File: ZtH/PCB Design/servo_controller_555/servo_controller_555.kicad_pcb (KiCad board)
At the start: 2 copper layers, 60 x 50 mm, 20 parts, among them J1 SERVO, J2 VIN, U1 LM555xN, U2 AMS1117

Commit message: a
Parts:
- moved U2 119.1 mm to (68.3, 85.0)
- moved D2 95.5 mm to (66.5, 72.0)
- moved C3 94.5 mm to (67.5, 77.0), turned to 180 degrees
- moved D3 92.9 mm to (68.0, 95.0), turned to 180 degrees
- moved D4 91.0 mm to (57.0, 93.5), turned to 180 degrees
- moved R3 88.4 mm to (62.0, 69.4), turned to -90 degrees
- moved U1 85.4 mm to (95.5, 93.1), turned to 180 degrees
- moved R4 78.9 mm to (68.5, 92.0), turned to 180 degrees
- moved C1 73.6 mm to (98.4, 90.6), turned to -90 degrees
- moved C2 73.0 mm to (90.4, 97.6)
- moved R2 64.7 mm to (83.8, 75.6)
- moved R1 62.6 mm to (83.9, 78.1)
- moved D1 56.5 mm to (83.9, 81.1)
- moved RV1 13.0 mm to (80.6, 107.5), turned to 90 degrees
- moved J1 1.46 mm to (105.0, 82.5)
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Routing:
- net +5V: track 0.00 -> 114.9 mm
- net GND: track 0.00 -> 58.1 mm, vias 0 -> 1
- net Net-(R2-Pad1): track 0.00 -> 34.0 mm
- net Net-(D1-K): track 0.00 -> 23.1 mm
- net +12V: track 0.00 -> 17.6 mm
- net Net-(D1-A): track 0.00 -> 16.5 mm
- net Net-(J1-Pin_3): track 0.00 -> 9.69 mm
- net Net-(D4-A): track 0.00 -> 7.62 mm
- net Net-(D2-K): track 0.00 -> 5.55 mm
- net Net-(D3-K): track 0.00 -> 3.41 mm
- added copper zone on B.Cu, net GND

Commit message: updated pcb
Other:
- board text added: "Theo Devos-Vernes c3479858 15/08/2026"
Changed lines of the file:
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@@
 	)
 	(paper "A4")
+	(title_block
+		(title "servo controller 555 pcb")
+		(company "NUTeams")
+		(comment 1 "Theo Devos-Vernes")
+		(comment 2 "c3479858")
+	)
 	(layers
 		(0 "F.Cu" signal)
@@
 		(layer "Edge.Cuts")
 	)
+	(gr_text "Theo Devos-Vernes\nc3479858\n15/08/2026"
+		(at 78 67 0)
+		(layer "F.SilkS")
+		(effects
+			(font
+				(size 1 1)
+				(thickness 0.1)
+			)
+			(justify left bottom)
+		)
+	)
 	(segment
 		(start 87.88 88)
@@
 	)
 	(segment
+		(start 71.5 85)
+		(end 79.58 93.08)
+		(width 0.2)
+		(layer "F.Cu")
+		(net "+5V")
+	)
+	(segment
+		(start 68.5375 77)
+		(end 68.5375 82.0375)
+		(width 0.4)
+		(layer "F.Cu")
+		(net "+5V")
+	)
+	(segment
 		(start 78.1 107.5)
 		(end 78.1 94.56)
@@
 	)
 	(segment
-		(start 80 93.08)
-		(end 87.88 93.08)
-		(width 0.2)
+		(start 68.5375 82.0375)
+		(end 71.5 85)
+		(width 0.4)
 		(layer "F.Cu")
 		(net "+5V")
 	)
 	(segment
-		(start 79.58 93.08)
-		(end 80 93.08)
+		(start 80 93.08)
+		(end 87.88 93.08)
 		(width 0.2)
 		(layer "F.Cu")
@@
 	)
 	(segment
-		(start 71.5 85)
-		(end 71.5 79.9625)
+		(start 79.58 93.08)
+		(end 80 93.08)
 		(width 0.2)
 		(layer "F.Cu")
@@
 	)
 	(segment
-		(start 71.5 85)
-		(end 79.58 93.08)
-		(width 0.2)
-		(layer "F.Cu")
-		(net "+5V")
-	)
-	(segment
 		(start 100 78.5)
 		(end 91.5 70)
@@
 		(width 0.2)
 		(layer "F.Cu")
-		(net "+5V")
-	)
-	(segment
-		(start 71.5 79.9625)
-		(end 68.5375 77)
-		(width 0.2)
-		(layer "F.Cu")

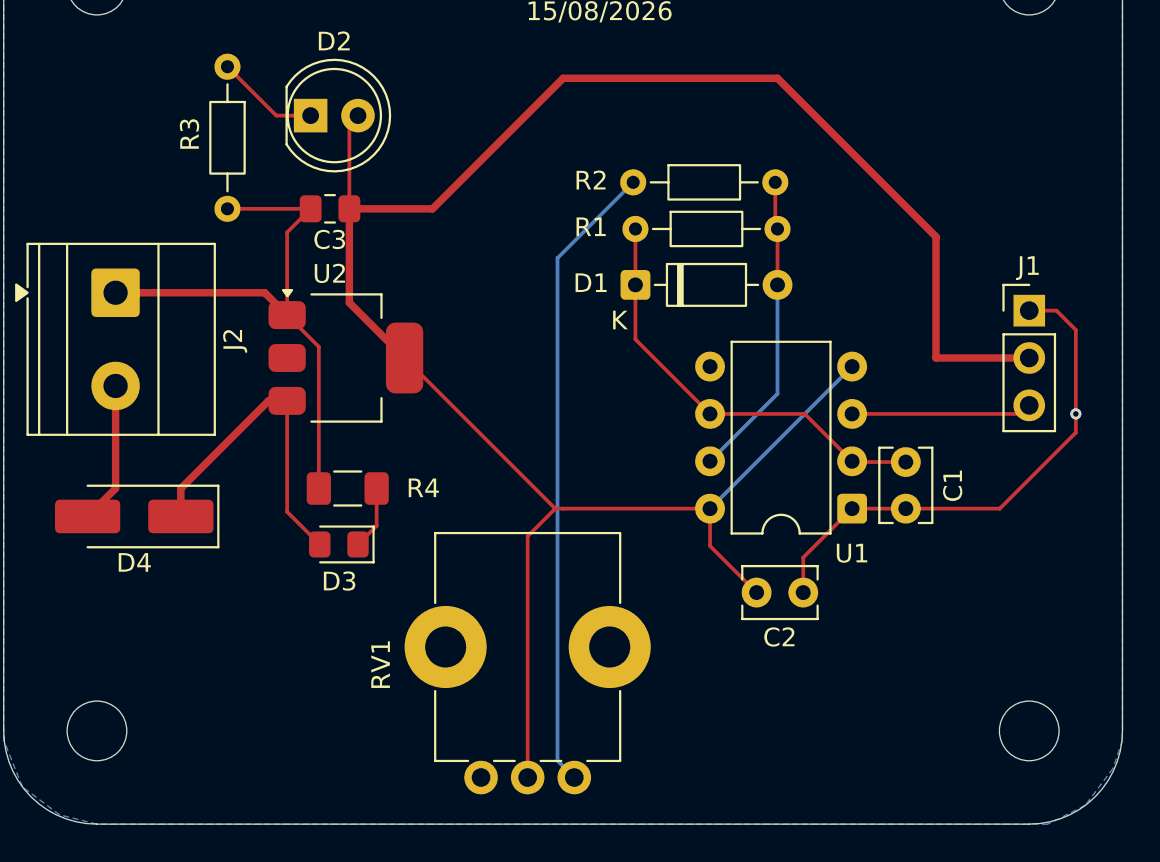
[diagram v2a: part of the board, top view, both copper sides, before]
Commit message: Adds gerbers and corrects minor routing issues
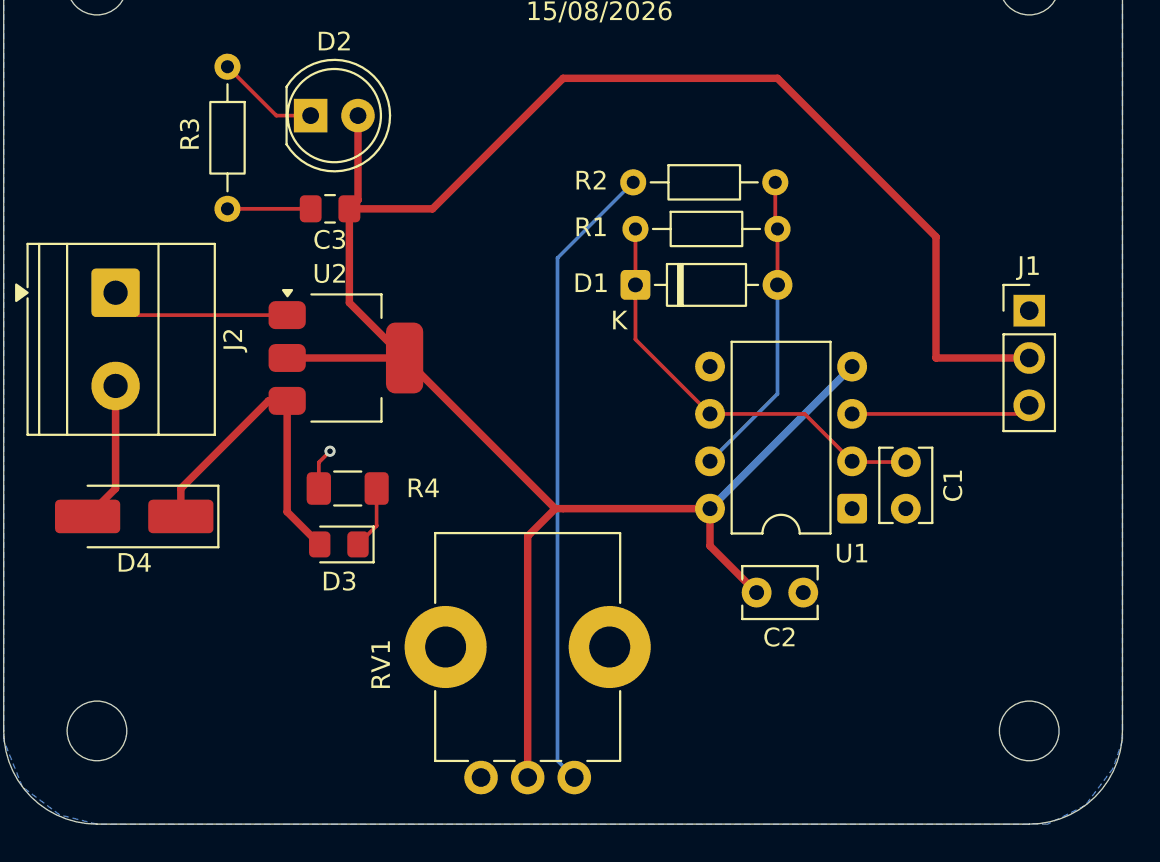
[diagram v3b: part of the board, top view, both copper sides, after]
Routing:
- net GND: track 58.1 -> 16.4 mm
- net +5V: track 114.9 -> 121.2 mm
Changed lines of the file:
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@@
 	)
 	(setup
+		(stackup
+			(layer "F.SilkS"
+				(type "Top Silk Screen")
+			)
+			(layer "F.Paste"
+				(type "Top Solder Paste")
+			)
+			(layer "F.Mask"
+				(type "Top Solder Mask")
+				(thickness 0.01)
+			)
+			(layer "F.Cu"
+				(type "copper")
+				(thickness 0.035)
+			)
+			(layer "dielectric 1"
+				(type "core")
+				(thickness 1.51)
+				(material "FR4")
+				(epsilon_r 4.5)
+				(loss_tangent 0.02)
+			)
+			(layer "B.Cu"
+				(type "copper")
+				(thickness 0.035)
+			)
+			(layer "B.Mask"
+				(type "Bottom Solder Mask")
+				(thickness 0.01)
+			)
+			(layer "B.Paste"
+				(type "Bottom Solder Paste")
+			)
+			(layer "B.SilkS"
+				(type "Bottom Silk Screen")
+			)
+			(copper_finish "None")
+			(dielectric_constraints no)
+		)
 		(pad_to_mask_clearance 0)
 		(allow_soldermask_bridges_in_footprints no)
@@
 		(capping no)
 		(filling no)
+		(zone_defaults)
 		(pcbplotparams
 			(layerselection 0x00000000_00000000_55555555_5755f5ff)
 			(plot_on_all_layers_selection 0x00000000_00000000_00000000_00000000)
 			(disableapertmacros no)
-			(usegerberextensions no)
+			(usegerberextensions yes)
 			(usegerberattributes yes)
 			(usegerberadvancedattributes yes)
@@
 			(outputformat 1)
 			(mirror no)
-			(drillshape 1)
+			(drillshape 0)
 			(scaleselection 1)
-			(outputdirectory "")
+			(outputdirectory "../servo_controller_555_gerbers/")
 		)
 	)
@@
 	)
 	(segment
-		(start 66.9 84.4)
-		(end 65.2 82.7)
+		(start 57.2 82.7)
+		(end 56 81.5)
 		(width 0.2)
 		(layer "F.Cu")
@@
 	)
 	(segment
-		(start 103.42 93.08)
-		(end 98.38 93.08)
-		(width 0.2)
-		(layer "F.Cu")
-		(net "GND")
-	)
-	(segment
-		(start 64 81.5)
-		(end 65.2 82.7)
-		(width 0.4)
-		(layer "F.Cu")
-		(net "GND")
-	)
-	(segment
-		(start 107.5 88)
-		(end 107.5 83.5)
-		(width 0.2)
-		(layer "F.Cu")
-		(net "GND")
-	)
-	(segment
-		(start 66.9 92)
-		(end 66.9 84.4)
-		(width 0.2)
-		(layer "F.Cu")
-		(net "GND")
-	)
-	(segment
 		(start 65.2 82.7)
-		(end 65.2 78.2625)
-		(width 0.2)
-		(layer "F.Cu")
-		(net "GND")
-	)
-	(segment
-		(start 92.88 95.7)
-		(end 95.5 93.08)
-		(width 0.2)
-		(layer "F.Cu")
-		(net "GND")
-	)
-	(segment
-		(start 56 81.5)
-		(end 64 81.5)
-		(width 0.4)
-		(layer "F.Cu")
-		(net "GND")
-	)
-	(segment
-		(start 107.5 88)
-		(end 107.5 89)
-		(width 0.2)
-		(layer "F.Cu")
-		(net "GND")
-	)
-	(segment
-		(start 106.46 82.46)
-		(end 105 82.46)
-		(width 0.2)
-		(layer "F.Cu")
-		(net "GND")
-	)
-	(segment
-		(start 107.5 89)
-		(end 103.42 93.08)
+		(end 57.2 82.7)
 		(width 0.2)
 		(layer "F.Cu")
@@
 	)
 	(segment
-		(start 107.5 83.5)
-		(end 106.46 82.46)
+		(start 66.9 90.6)
+		(end 67.5 90)
 		(width 0.2)
 		(layer "F.Cu")
@@
 	)
 	(segment
-		(start 92.88 97.58)
-		(end 92.88 95.7)
-		(width 0.2)
-		(layer "F.Cu")
-		(net "GND")
-	)
-	(segment
-		(start 95.5 93.08)
-		(end 98.38 93.08)
-		(width 0.2)
-		(layer "F.Cu")
-		(net "GND")
-	)
-	(segment
-		(start 65.2 78.2625)
-		(end 66.4625 77)
+		(start 66.9 92)
+		(end 66.9 90.6)
 		(width 0.2)
 		(layer "F.Cu")
@@
 	)
 	(via
-		(at 107.5 88)
+		(at 67.5 90)
 		(size 0.6)
 		(drill 0.3)
@@
 	)
 	(segment
+		(start 68.5375 77)
+		(end 69 76.5375)
+		(width 0.4)
+		(layer "F.Cu")
+		(net "+5V")
+	)
+	(segment
 		(start 100 85)
 		(end 100 78.5)
@@
 		(start 87.88 93.08)
 		(end 87.88 95.08)
-		(width 0.2)
+		(width 0.4)
 		(layer "F.Cu")
 		(net "+5V")
@@
 		(start 87.88 95.08)
 		(end 90.38 97.58)
-		(width 0.2)
+		(width 0.4)
 		(layer "F.Cu")
 		(net "+5V")
@@
 		(start 71.5 85)
 		(end 79.58 93.08)
-		(width 0.2)
+		(width 0.4)
 		(layer "F.Cu")
 		(net "+5V")
@@
 		(start 78.1 107.5)
 		(end 78.1 94.56)
-		(width 0.2)
+		(width 0.4)
 		(layer "F.Cu")
 		(net "+5V")
@@
 	)
 	(segment
-		(start 68.5375 72.4625)
-		(end 69 72)
-		(width 0.2)
-		(layer "F.Cu")
-		(net "+5V")
-	)
-	(segment
-		(start 68.5375 77)
-		(end 68.5375 72.4625)
-		(width 0.2)
-		(layer "F.Cu")
-		(net "+5V")
-	)
-	(segment
 		(start 68.5375 82.0375)
 		(end 71.5 85)
@@
 		(start 80 93.08)
 		(end 87.88 93.08)
-		(width 0.2)
+		(width 0.4)
+		(layer "F.Cu")
+		(net "+5V")
+	)
+	(segment
+		(start 69 76.5375)
+		(end 69 72)
+		(width 0.4)
 		(layer "F.Cu")
 		(net "+5V")
@@
 		(start 79.58 93.08)
 		(end 80 93.08)
-		(width 0.2)
+		(width 0.4)
 		(layer "F.Cu")
 		(net "+5V")
@@
 	)
 	(segment
+		(start 65.2 85)
+		(end 71.5 85)
+		(width 0.4)
+		(layer "F.Cu")
+		(net "+5V")
+	)
+	(segment
 		(start 100 78.5)
 		(end 91.5 70)
@@
 		(start 78.1 94.56)
 		(end 79.58 93.08)
-		(width 0.2)
+		(width 0.4)
 		(layer "F.Cu")
 		(net "+5V")
@@
 		(start 95.5 85.46)
 		(end 87.88 93.08)
-		(width 0.2)
+		(width 0.4)
 		(layer "B.Cu")
 		(net "+5V")
@@
 		(start 65.2 93.25)
 		(end 66.95 95)
-		(width 0.2)
+		(width 0.4)
 		(layer "F.Cu")
 		(net "+12V")
@@
 		(start 65.2 87.3)
 		(end 65.2 93.25)
-		(width 0.2)
+		(width 0.4)
 		(layer "F.Cu")
 		(net "+12V")

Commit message: pcb update
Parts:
- added G***: LOGO, LOGO, F.Cu at (96.5, 104.5)
- added G***: LOGO, LOGO, B.Cu at (65.0, 105.0)
- added ThinkFast: LOGO, LOGO, B.Cu at (65.0, 98.0)
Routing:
- net GND: track 16.4 -> 6.95 mm, vias 1 -> 2
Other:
- board text added: "NU Teams 555 Servo Driver v1"
